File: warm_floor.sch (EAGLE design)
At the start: 30 parts, among them K1 G2R, Q1 BSS123, T1 BC847, T2 BC847, T3 BC847, X1 53047-04, X3 DG3XX-03-3.5, X4 DG3XX-02-3.5

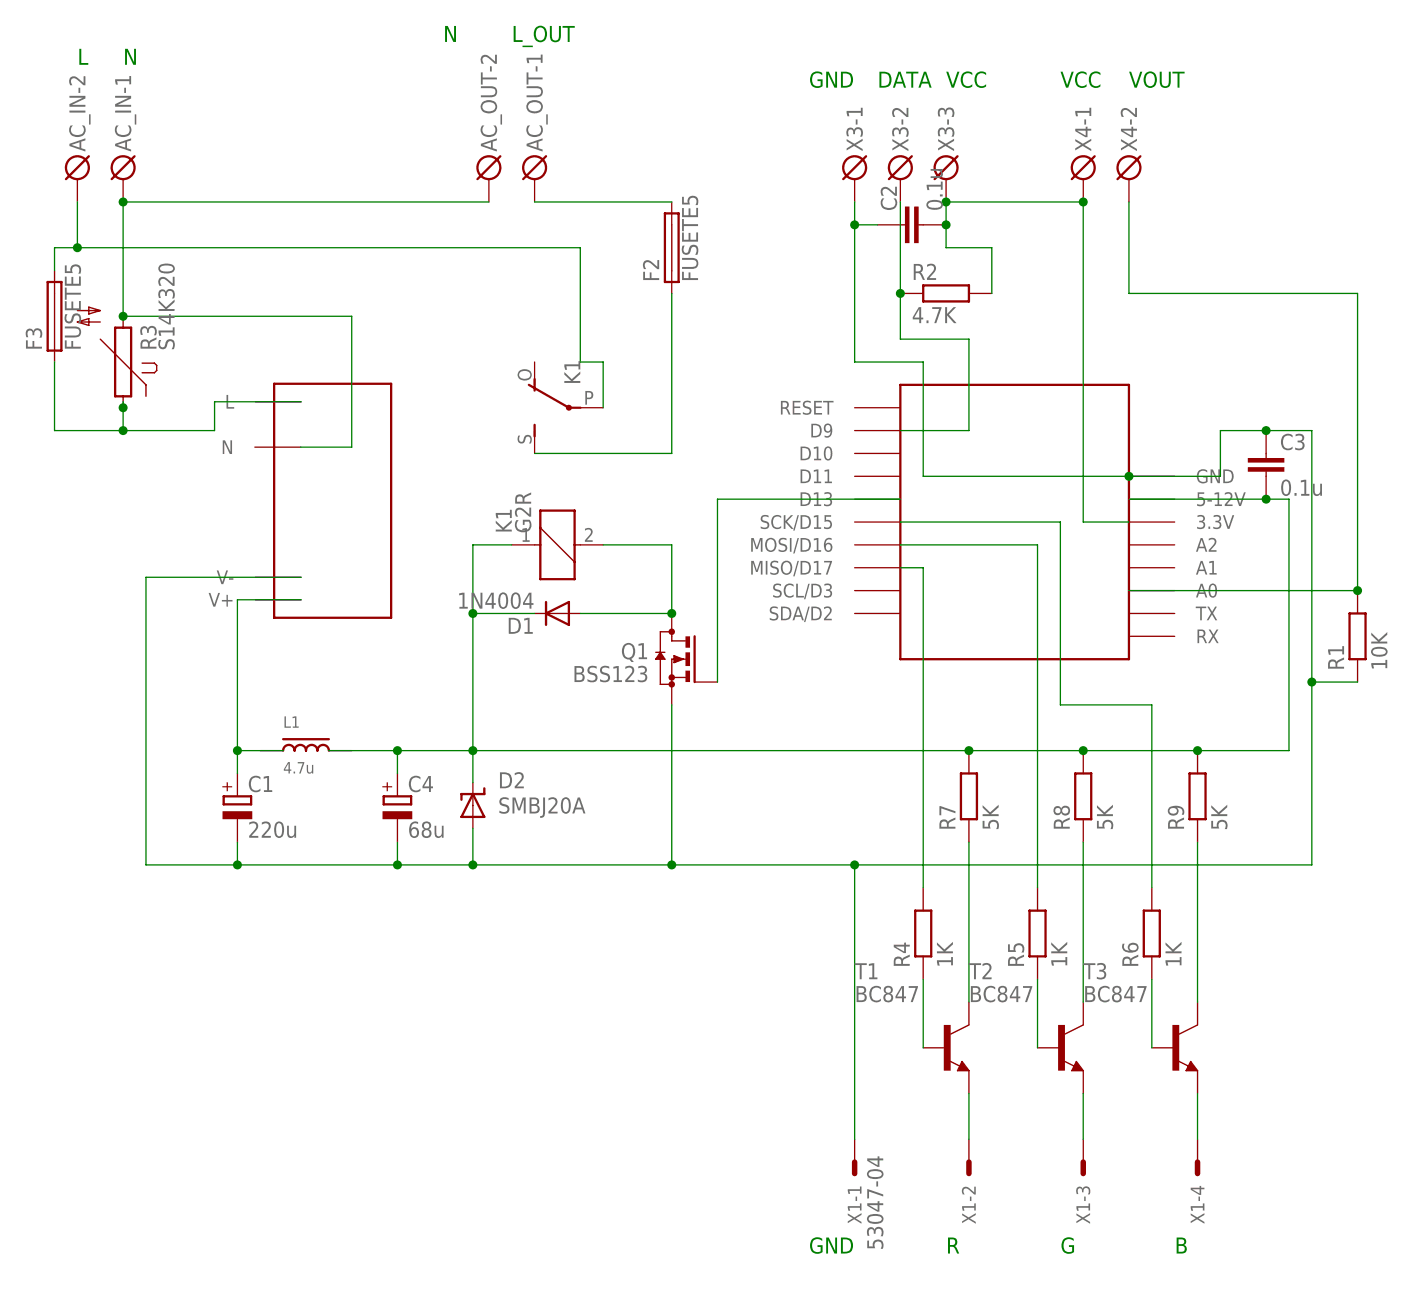
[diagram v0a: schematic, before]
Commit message: linked all wires
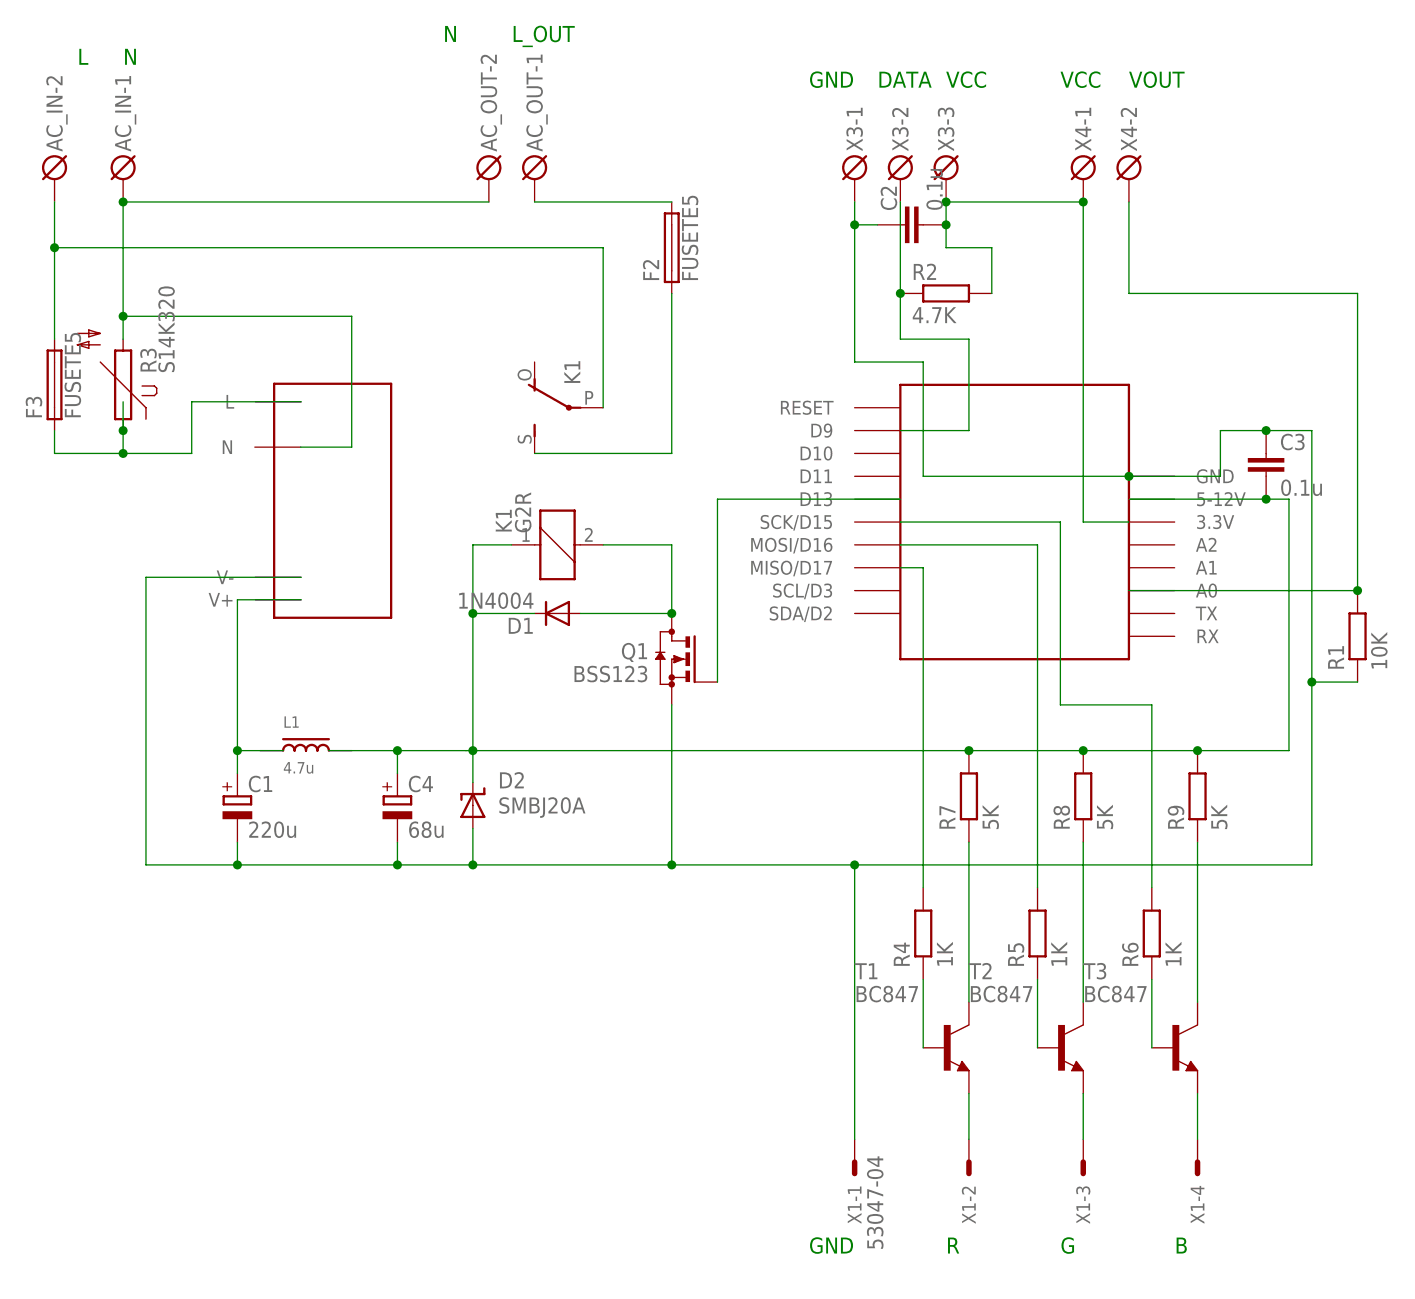
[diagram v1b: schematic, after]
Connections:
- new net N$1: C1.+, L1.P$1, U$2.V+
- new net N$2: F3.1, R3.1, U$2.L
- new net N$3: F2.1, K12.S
- new net N$5: AC_OUT-1.KL, F2.2
- net L: no longer AC_OUT-1.KL, F2.1, F2.2, F3.1, K12.S, R3.1, U$2.L
- net VCC: no longer C1.+, L1.P$1, U$2.V+
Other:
- moved on the sheet: AC_IN-2, F3, R3

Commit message: Add files via upload
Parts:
- removed R3: S14K320, varistor:S14K320
- added F1: (no value), fuse:TR5
- added R10: S10K385, varistor:S10K385
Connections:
- net N$3 renamed RELAY_OUT
- net N$5 renamed WF_L
- new net PS_L: F1.1, F3.1, U$2.L
- net L: now also F1.2; no longer F3.2
- net N: now also R10.2; no longer R3.2
- net N$2: now also F3.2, R10.1; no longer F3.1, R3.1, U$2.L
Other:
- moved on the sheet: C2, F3, R2, X3-1, X3-2, X3-3

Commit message: Last G2R version
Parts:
- removed AC_IN, AC_OUT: DG3XX-02-3.5, degson:DG3XX-02-3.5
- added X5, X6: DG3XX-025.0, degson:DG3XX-025.0
- D1: value 1N4004 -> (none); device diode:1N4004 -> diode:DIODE-SOD123
- D2: value SMBJ20A -> SMBJ15A
- F1: value (none) -> FUSETE5; device fuse:TR5 -> fuse:FUSETE5
- R2: device resistor:R-EU_R1206 -> rcl:R-EU_R0805
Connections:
- net L: now also X5-2.KL; no longer AC_IN-2.KL
- net N: now also X5-1.KL, X6-2.KL; no longer AC_IN-1.KL, AC_OUT-2.KL
- net WF_L: now also X6-1.KL; no longer AC_OUT-1.KL
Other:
- moved on the sheet: C2, R2, X3-1, X3-2, X3-3

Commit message: Pre-publish commit
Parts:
- removed X6: DG3XX-025.0, degson:DG3XX-025.0
- added C5: 10u, rcl:CPOL-EUE2.5-6
- added D3: (no value), diode:SUPPRESSOR-SMBJ
- added X2: DG3XX-025.0, degson:DG3XX-025.0
- C3: device rcl:C-EUC1206 -> rcl:C-EUC0805
- K1: value G2R -> G5Q-1A; device relay:G2R -> relay:G5Q-1A
- R1: device resistor:R-EU_R1206 -> rcl:R-EU_R0805
- X3: value DG3XX-03-3.5 -> DG3XX-025.0; device degson:DG3XX-03-3.5 -> degson:DG3XX-025.0
- X4: value DG3XX-02-3.5 -> DG3XX-03-3.5; device degson:DG3XX-02-3.5 -> degson:DG3XX-03-3.5
- X5: value DG3XX-025.0 -> DG3XX-02-3.5; device degson:DG3XX-025.0 -> degson:DG3XX-02-3.5
- renumbered R10 to R3
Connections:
- removed net RELAY_OUT: F2.1, K12.S
- removed net WF_L: F2.2, X6-1.KL
- new net N$5: F2.1, K1G$2.P
- new net N$6: K1G$2.S, X3-1.KL
- new net N$7: D1.A, D3.A
- net 3.3V: now also X4-3.KL, X5-1.KL; no longer X3-3.KL, X4-1.KL
- net DATA: now also X4-2.KL; no longer X3-2.KL
- net GND: now also C5.-, X4-1.KL; no longer X3-1.KL
- net L: now also F2.2, X2-2.KL; no longer K12.P, X5-2.KL
- net N: now also X2-1.KL, X3-2.KL; no longer X5-1.KL, X6-2.KL
- net N$4: now also D3.C, K1G$1.1; no longer D1.A, K11.2
- net NTC: now also X5-2.KL; no longer X4-2.KL
- net VCC: now also C5.+, K1G$1.2; no longer K11.1
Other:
- moved on the sheet: D1, F2, X3-1, X3-2, X4-1, X4-2, X5-1, X5-2
